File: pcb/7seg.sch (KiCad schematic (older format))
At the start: 28 parts, among them Q10 2SC1815, Q11 2SC1815, Q12 2SC1815, Q13 2SC1815, Q14 2SC1815, Q9 2SC1815, U7 7seg-2digit-ca, U8 7seg-2digit-ca, U9 7seg-2digit-ca

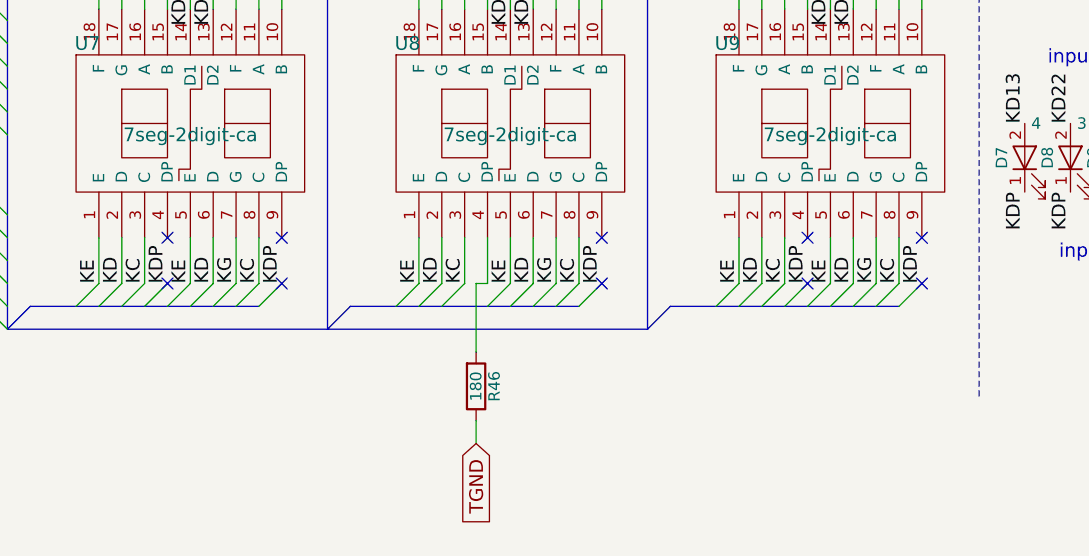
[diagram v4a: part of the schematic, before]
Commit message: wire に未接続の設定をしていたら文句を言われたので，wireの未接続を削除。
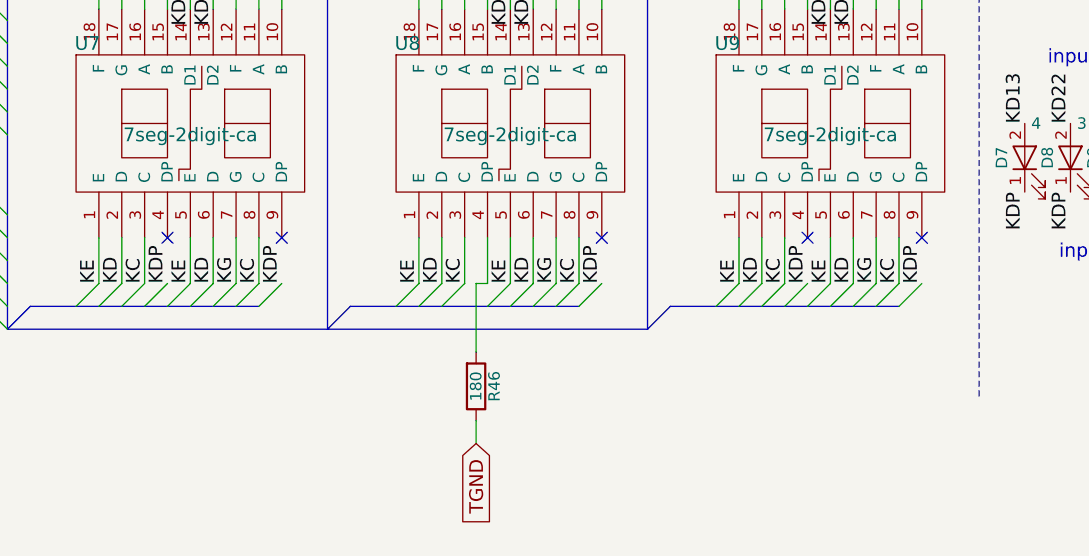
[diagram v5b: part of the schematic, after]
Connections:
- no-connect marks 10 -> 5
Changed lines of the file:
@@
 Entry Wire Line
 	5050 4000 4950 3900
-NoConn ~ 6250 3900
-NoConn ~ 5750 3900
-NoConn ~ 7650 3900
-NoConn ~ 9050 3900
 Text Label 4450 2450 2    60   ~ 0
 PB7
@@
 Text Notes 4450 3400 0    60   ~ 0
 input H.
-NoConn ~ 8550 3900
 Text Notes 9650 3800 0    60   ~ 0
 input L.
@@
 	1    0    0    -1
 $EndComp
-Wire Wire Line
-	3300 3900 4950 3900
-Wire Wire Line
-	3700 4000 4950 4000
-Wire Wire Line
-	2900 3800 4950 3800
-Wire Notes Line
-	9300 2100 9300 4400
-Wire Wire Line
-	7100 3900 7100 4200
-Wire Wire Line
-	7150 3900 7100 3900
-Wire Wire Line
-	7150 3700 7150 3900
-Wire Wire Line
-	4800 2450 4950 2450
-Wire Wire Line
-	1700 3500 4950 3500
-Wire Wire Line
-	2100 3600 4950 3600
-Wire Bus Line
-	7850 4100 7850 2550
-Wire Bus Line
-	7950 4000 8950 4000
-Wire Bus Line
-	7950 2450 8950 2450
-Wire Wire Line
-	8250 3900 8250 3700
-Wire Wire Line
-	8350 3900 8350 3700
-Wire Wire Line
-	8450 3900 8450 3700
-Wire Wire Line
-	8650 3900 8650 3700
-Wire Wire Line
-	8750 3900 8750 3700
-Wire Wire Line
-	8850 3900 8850 3700
-Wire Wire Line
-	8950 3900 8950 3700
-Wire Wire Line
-	8250 2550 8250 2700
-Wire Wire Line
-	8350 2550 8350 2700
-Wire Wire Line
-	8450 2550 8450 2700
-Wire Wire Line
-	8550 2550 8550 2700
-Wire Wire Line
-	8650 2550 8650 2700
-Wire Wire Line
-	8750 2550 8750 2700
-Wire Wire Line
-	8850 2550 8850 2700
-Wire Wire Line
-	8950 2550 8950 2700
-Wire Wire Line
-	9050 2550 9050 2700
-Wire Bus Line
-	5050 4100 7850 4100
-Wire Bus Line
-	6450 2550 6450 4100
-Wire Bus Line
-	6550 4000 7550 4000
-Wire Bus Line
-	6550 2450 7550 2450
-Wire Wire Line
-	6850 3900 6850 3700
-Wire Wire Line
-	6950 3900 6950 3700
-Wire Wire Line
-	7050 3900 7050 3700
-Wire Wire Line
-	7250 3900 7250 3700
-Wire Wire Line
-	7350 3900 7350 3700
-Wire Wire Line
-	7450 3900 7450 3700
-Wire Wire Line
-	7550 3900 7550 3700
-Wire Wire Line
-	6850 2550 6850 2700
-Wire Wire Line
-	6950 2550 6950 2700
-Wire Wire Line
-	7050 2550 7050 2700
-Wire Wire Line
-	7150 2550 7150 2700
-Wire Wire Line
-	7250 2550 7250 2700
-Wire Wire Line
-	7350 2550 7350 2700
-Wire Wire Line
-	7450 2550 7450 2700
-Wire Wire Line
-	7550 2550 7550 2700
-Wire Wire Line
-	7650 2550 7650 2700
-Wire Wire Line
-	4950 2650 4800 2650
-Wire Wire Line
-	4950 3150 4800 3150
-Wire Wire Line
-	4950 2550 4800 2550
-Wire Wire Line
-	4950 2950 4800 2950
-Wire Wire Line
-	4950 2850 4800 2850
-Wire Wire Line
-	4950 2750 4800 2750
-Wire Wire Line
-	4950 3050 4800 3050
-Wire Wire Line
-	4250 3150 4500 3150
-Wire Wire Line
-	4250 3050 4500 3050
-Wire Wire Line
-	4250 2950 4500 2950
-Wire Wire Line
-	4250 2850 4500 2850
-Wire Wire Line
-	4250 2750 4500 2750
-Wire Wire Line
-	4250 2650 4500 2650
-Wire Wire Line
-	4250 2550 4500 2550
-Wire Bus Line
-	5050 2550 5050 4100
-Wire Bus Line
-	5150 4000 6150 4000
-Wire Bus Line
-	5150 2450 6150 2450
-Wire Wire Line
-	5450 3900 5450 3700
-Wire Wire Line
-	5550 3900 5550 3700
-Wire Wire Line
-	5650 3900 5650 3700
-Wire Wire Line
-	5850 3900 5850 3700
-Wire Wire Line
-	5950 3900 5950 3700
-Wire Wire Line
-	6050 3900 6050 3700
-Wire Wire Line
-	6150 3900 6150 3700
-Wire Wire Line
-	5450 2550 5450 2700
-Wire Wire Line
-	5550 2550 5550 2700
-Wire Wire Line
-	5650 2550 5650 2700
-Wire Wire Line
-	5750 2550 5750 2700
-Wire Wire Line
-	5850 2550 5850 2700
-Wire Wire Line
-	5950 2550 5950 2700
-Wire Wire Line
-	6050 2550 6050 2700
-Wire Wire Line
-	6150 2550 6150 2700
-Wire Wire Line
-	6250 2550 6250 2700
-Wire Wire Line
-	4250 2450 4500 2450
-Wire Wire Line
-	7100 4600 7100 4500
-Wire Wire Line
-	1400 2650 1300 2650
-Wire Wire Line
-	1300 2750 1800 2750
-Wire Wire Line
-	1300 2850 2200 2850
-Wire Wire Line
-	1300 2950 2600 2950
-Wire Wire Line
-	3000 3050 1300 3050
-Wire Wire Line
-	1300 3150 3400 3150
-Wire Wire Line
-	850  3150 1000 3150
-Wire Wire Line
-	850  3050 1000 3050
-Wire Wire Line
-	1000 2650 850  2650
-Wire Wire Line
-	850  2750 1000 2750
-Wire Wire Line
-	1000 2850 850  2850
-Wire Wire Line
-	850  2950 1000 2950
-Wire Wire Line
-	1700 2850 1700 3500
-Wire Wire Line
-	2100 3600 2100 2950
-Wire Wire Line
-	2500 3700 2500 3050
-Wire Wire Line
-	2900 3800 2900 3150
-Wire Wire Line
-	3300 3250 3300 3900
-Wire Wire Line
-	3700 3350 3700 4000
-Wire Wire Line
-	3700 1800 3700 2950
-Wire Wire Line
-	1700 1950 3700 1950
-Wire Wire Line
-	3300 1950 3300 2850
-Wire Wire Line
-	2900 1950 2900 2750
-Connection ~ 3300 1950
-Wire Wire Line
-	2500 1950 2500 2650
-Connection ~ 2900 1950
-Wire Wire Line
-	2100 1950 2100 2550
-Connection ~ 2500 1950
-Wire Wire Line
-	1700 1950 1700 2450
-Connection ~ 2100 1950
-Connection ~ 3700 1950
 Text Label 4850 3700 2    60   ~ 0
 KD22
-Wire Wire Line
-	2500 3700 4950 3700
 Text Notes 800  3300 0    60   ~ 0
 flow ->
@@
 Text GLabel 3700 1800 2    60   Input ~ 0
 TVCC
+Wire Wire Line
+	3300 3900 4950 3900
+Wire Wire Line
+	3700 4000 4950 4000
+Wire Wire Line
+	2900 3800 4950 3800
+Wire Notes Line
+	9300 2100 9300 4400
+Wire Wire Line
+	7100 3900 7100 4200
+Wire Wire Line
+	7150 3900 7100 3900
+Wire Wire Line
+	7150 3700 7150 3900
+Wire Wire Line
+	4800 2450 4950 2450
+Wire Wire Line
+	1700 3500 4950 3500
+Wire Wire Line
+	2100 3600 4950 3600
+Wire Bus Line
+	7850 4100 7850 2550
+Wire Bus Line
+	7950 4000 8950 4000
+Wire Bus Line
+	7950 2450 8950 2450
+Wire Wire Line
+	8250 3900 8250 3700
+Wire Wire Line
+	8350 3900 8350 3700
+Wire Wire Line
+	8450 3900 8450 3700
+Wire Wire Line
+	8650 3900 8650 3700
+Wire Wire Line
+	8750 3900 8750 3700
+Wire Wire Line
+	8850 3900 8850 3700
+Wire Wire Line
+	8950 3900 8950 3700
+Wire Wire Line
+	8250 2550 8250 2700
+Wire Wire Line
+	8350 2550 8350 2700
+Wire Wire Line
+	8450 2550 8450 2700
+Wire Wire Line
+	8550 2550 8550 2700
+Wire Wire Line
+	8650 2550 8650 2700
+Wire Wire Line
+	8750 2550 8750 2700
+Wire Wire Line
+	8850 2550 8850 2700
+Wire Wire Line
+	8950 2550 8950 2700
+Wire Wire Line
+	9050 2550 9050 2700
+Wire Bus Line
+	5050 4100 7850 4100
+Wire Bus Line
+	6450 2550 6450 4100
+Wire Bus Line
+	6550 4000 7550 4000
+Wire Bus Line
+	6550 2450 7550 2450
+Wire Wire Line
+	6850 3900 6850 3700
+Wire Wire Line
+	6950 3900 6950 3700
+Wire Wire Line
+	7050 3900 7050 3700
+Wire Wire Line
+	7250 3900 7250 3700
+Wire Wire Line
+	7350 3900 7350 3700
+Wire Wire Line
+	7450 3900 7450 3700
+Wire Wire Line
+	7550 3900 7550 3700
+Wire Wire Line
+	6850 2550 6850 2700
+Wire Wire Line
+	6950 2550 6950 2700
+Wire Wire Line
+	7050 2550 7050 2700
+Wire Wire Line
+	7150 2550 7150 2700
+Wire Wire Line
+	7250 2550 7250 2700
+Wire Wire Line
+	7350 2550 7350 2700
+Wire Wire Line
+	7450 2550 7450 2700
+Wire Wire Line
+	7550 2550 7550 2700
+Wire Wire Line
+	7650 2550 7650 2700
+Wire Wire Line
+	4950 2650 4800 2650
+Wire Wire Line
+	4950 3150 4800 3150
+Wire Wire Line
+	4950 2550 4800 2550
+Wire Wire Line
+	4950 2950 4800 2950
+Wire Wire Line
+	4950 2850 4800 2850
+Wire Wire Line
+	4950 2750 4800 2750
+Wire Wire Line
+	4950 3050 4800 3050
+Wire Wire Line
+	4250 3150 4500 3150
+Wire Wire Line
+	4250 3050 4500 3050
+Wire Wire Line
+	4250 2950 4500 2950
+Wire Wire Line
+	4250 2850 4500 2850
+Wire Wire Line
+	4250 2750 4500 2750
+Wire Wire Line
+	4250 2650 4500 2650
+Wire Wire Line
+	4250 2550 4500 2550
+Wire Bus Line
+	5050 2550 5050 4100
+Wire Bus Line
+	5150 4000 6150 4000
+Wire Bus Line
+	5150 2450 6150 2450
+Wire Wire Line
+	5450 3900 5450 3700
+Wire Wire Line
+	5550 3900 5550 3700
+Wire Wire Line
+	5650 3900 5650 3700
+Wire Wire Line
+	5850 3900 5850 3700
+Wire Wire Line
+	5950 3900 5950 3700
+Wire Wire Line
+	6050 3900 6050 3700
+Wire Wire Line
+	6150 3900 6150 3700
+Wire Wire Line
+	5450 2550 5450 2700
+Wire Wire Line
+	5550 2550 5550 2700
+Wire Wire Line
+	5650 2550 5650 2700
+Wire Wire Line
+	5750 2550 5750 2700
+Wire Wire Line
+	5850 2550 5850 2700
+Wire Wire Line
+	5950 2550 5950 2700
+Wire Wire Line
+	6050 2550 6050 2700
+Wire Wire Line
+	6150 2550 6150 2700
+Wire Wire Line
+	6250 2550 6250 2700
+Wire Wire Line
+	4250 2450 4500 2450
+Wire Wire Line
+	7100 4600 7100 4500
+Wire Wire Line
+	1400 2650 1300 2650
+Wire Wire Line
+	1300 2750 1800 2750
+Wire Wire Line
+	1300 2850 2200 2850
+Wire Wire Line
+	1300 2950 2600 2950
+Wire Wire Line
+	3000 3050 1300 3050
+Wire Wire Line
+	1300 3150 3400 3150
+Wire Wire Line
+	850  3150 1000 3150
+Wire Wire Line
+	850  3050 1000 3050
+Wire Wire Line
+	1000 2650 850  2650
+Wire Wire Line
+	850  2750 1000 2750
+Wire Wire Line
+	1000 2850 850  2850
+Wire Wire Line
+	850  2950 1000 2950
+Wire Wire Line
+	1700 2850 1700 3500
+Wire Wire Line
+	2100 3600 2100 2950
+Wire Wire Line
+	2500 3700 2500 3050
+Wire Wire Line
+	2900 3800 2900 3150
+Wire Wire Line
+	3300 3250 3300 3900
+Wire Wire Line
+	3700 3350 3700 4000
+Wire Wire Line
+	3700 1800 3700 2950
+Wire Wire Line
+	1700 1950 3700 1950
+Wire Wire Line
+	3300 1950 3300 2850
+Wire Wire Line
+	2900 1950 2900 2750
+Connection ~ 3300 1950
+Wire Wire Line
+	2500 1950 2500 2650
+Connection ~ 2900 1950
+Wire Wire Line
+	2100 1950 2100 2550
+Connection ~ 2500 1950
+Wire Wire Line
+	1700 1950 1700 2450
+Connection ~ 2100 1950
+Connection ~ 3700 1950
+Wire Wire Line
+	2500 3700 4950 3700
 $EndSCHEMATC

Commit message: 抵抗を 6.3mm の 1 / 4 W の抵抗に変更。
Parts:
- D10, D7, D8, D9: footprint (none) -> LEDs:LED_D5.0mm
- R32, R33, R34, R35, R36, R37, R38, R39, R40, R41, R42, R43, R44, R45, R46: footprint (none) -> Resistors_THT:R_Axial_DIN0207_L6.3mm_D2.5mm_P7.62mm_Horizontal
- U7, U8, U9: footprint (none) -> freq-counter:PARA_LIGHT-552SRD
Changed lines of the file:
@@
 F 0 "U7" H 5400 3550 60  0000 C CNN
 F 1 "7seg-2digit-ca" H 5850 3150 60  0000 C CNN
-F 2 "" H 6100 3300 60  0001 C CNN
+F 2 "freq-counter:PARA_LIGHT-552SRD" H 6100 3300 60  0001 C CNN
 F 3 "" H 6100 3300 60  0001 C CNN
 	1    5850 3200
@@
 F 0 "R39" V 4700 2400 50  0000 C CNN
 F 1 "33" V 4650 2550 50  0000 C CNN
-F 2 "" V 4580 2550 50  0001 C CNN
+F 2 "Resistors_THT:R_Axial_DIN0207_L6.3mm_D2.5mm_P7.62mm_Horizontal" V 4580 2550 50  0001 C CNN
 F 3 "" H 4650 2550 50  0001 C CNN
 	1    4650 2550
@@
 F 0 "R40" V 4700 2500 50  0000 C CNN
 F 1 "33" V 4650 2650 50  0000 C CNN
-F 2 "" V 4580 2650 50  0001 C CNN
+F 2 "Resistors_THT:R_Axial_DIN0207_L6.3mm_D2.5mm_P7.62mm_Horizontal" V 4580 2650 50  0001 C CNN
 F 3 "" H 4650 2650 50  0001 C CNN
 	1    4650 2650
@@
 F 0 "R41" V 4700 2600 50  0000 C CNN
 F 1 "33" V 4650 2750 50  0000 C CNN
-F 2 "" V 4580 2750 50  0001 C CNN
+F 2 "Resistors_THT:R_Axial_DIN0207_L6.3mm_D2.5mm_P7.62mm_Horizontal" V 4580 2750 50  0001 C CNN
 F 3 "" H 4650 2750 50  0001 C CNN
 	1    4650 2750
@@
 F 0 "R42" V 4700 2700 50  0000 C CNN
 F 1 "33" V 4650 2850 50  0000 C CNN
-F 2 "" V 4580 2850 50  0001 C CNN
+F 2 "Resistors_THT:R_Axial_DIN0207_L6.3mm_D2.5mm_P7.62mm_Horizontal" V 4580 2850 50  0001 C CNN
 F 3 "" H 4650 2850 50  0001 C CNN
 	1    4650 2850
@@
 F 0 "R43" V 4700 2800 50  0000 C CNN
 F 1 "33" V 4650 2950 50  0000 C CNN
-F 2 "" V 4580 2950 50  0001 C CNN
+F 2 "Resistors_THT:R_Axial_DIN0207_L6.3mm_D2.5mm_P7.62mm_Horizontal" V 4580 2950 50  0001 C CNN
 F 3 "" H 4650 2950 50  0001 C CNN
 	1    4650 2950
@@
 F 0 "R44" V 4700 2900 50  0000 C CNN
 F 1 "33" V 4650 3050 50  0000 C CNN
-F 2 "" V 4580 3050 50  0001 C CNN
+F 2 "Resistors_THT:R_Axial_DIN0207_L6.3mm_D2.5mm_P7.62mm_Horizontal" V 4580 3050 50  0001 C CNN
 F 3 "" H 4650 3050 50  0001 C CNN
 	1    4650 3050
@@
 F 0 "R45" V 4700 3000 50  0000 C CNN
 F 1 "33" V 4650 3150 50  0000 C CNN
-F 2 "" V 4580 3150 50  0001 C CNN
+F 2 "Resistors_THT:R_Axial_DIN0207_L6.3mm_D2.5mm_P7.62mm_Horizontal" V 4580 3150 50  0001 C CNN
 F 3 "" H 4650 3150 50  0001 C CNN
 	1    4650 3150
@@
 F 0 "U8" H 6800 3550 60  0000 C CNN
 F 1 "7seg-2digit-ca" H 7250 3150 60  0000 C CNN
-F 2 "" H 7500 3300 60  0001 C CNN
+F 2 "freq-counter:PARA_LIGHT-552SRD" H 7500 3300 60  0001 C CNN
 F 3 "" H 7500 3300 60  0001 C CNN
 	1    7250 3200
@@
 F 0 "U9" H 8200 3550 60  0000 C CNN
 F 1 "7seg-2digit-ca" H 8650 3150 60  0000 C CNN
-F 2 "" H 8900 3300 60  0001 C CNN
+F 2 "freq-counter:PARA_LIGHT-552SRD" H 8900 3300 60  0001 C CNN
 F 3 "" H 8900 3300 60  0001 C CNN
 	1    8650 3200
@@
 F 0 "D8" H 9700 3450 50  0000 C CNN
 F 1 "3" V 9850 3300 50  0000 C CNN
-F 2 "" H 9700 3350 50  0001 C CNN
+F 2 "LEDs:LED_D5.0mm" H 9700 3350 50  0001 C CNN
 F 3 "" H 9700 3350 50  0001 C CNN
 	1    9700 3350
@@
 F 0 "D9" H 9900 3450 50  0000 C CNN
 F 1 "2" V 10050 3300 50  0000 C CNN
-F 2 "" H 9900 3350 50  0001 C CNN
+F 2 "LEDs:LED_D5.0mm" H 9900 3350 50  0001 C CNN
 F 3 "" H 9900 3350 50  0001 C CNN
 	1    9900 3350
@@
 F 0 "D7" H 9500 3450 50  0000 C CNN
 F 1 "4" V 9650 3300 50  0000 C CNN
-F 2 "" H 9500 3350 50  0001 C CNN
+F 2 "LEDs:LED_D5.0mm" H 9500 3350 50  0001 C CNN
 F 3 "" H 9500 3350 50  0001 C CNN
 	1    9500 3350
@@
 F 0 "D10" H 10100 3450 50  0000 C CNN
 F 1 "1" V 10250 3300 50  0000 C CNN
-F 2 "" H 10100 3350 50  0001 C CNN
+F 2 "LEDs:LED_D5.0mm" H 10100 3350 50  0001 C CNN
 F 3 "" H 10100 3350 50  0001 C CNN
 	1    10100 3350
@@
 F 0 "R46" V 7180 4350 50  0000 C CNN
 F 1 "180" V 7100 4350 50  0000 C CNN
-F 2 "" V 7030 4350 50  0001 C CNN
+F 2 "Resistors_THT:R_Axial_DIN0207_L6.3mm_D2.5mm_P7.62mm_Horizontal" V 7030 4350 50  0001 C CNN
 F 3 "" H 7100 4350 50  0001 C CNN
 	1    7100 4350
@@
 F 0 "R38" V 4700 2300 50  0000 C CNN
 F 1 "330" V 4650 2450 50  0000 C CNN
-F 2 "" V 4580 2450 50  0001 C CNN
+F 2 "Resistors_THT:R_Axial_DIN0207_L6.3mm_D2.5mm_P7.62mm_Horizontal" V 4580 2450 50  0001 C CNN
 F 3 "" H 4650 2450 50  0001 C CNN
 	1    4650 2450
@@
 F 0 "R32" V 1200 2500 50  0000 C CNN
 F 1 "10k" V 1150 2650 50  0000 C CNN
-F 2 "" V 1080 2650 50  0001 C CNN
+F 2 "Resistors_THT:R_Axial_DIN0207_L6.3mm_D2.5mm_P7.62mm_Horizontal" V 1080 2650 50  0001 C CNN
 F 3 "" H 1150 2650 50  0001 C CNN
 	1    1150 2650
@@
 F 0 "R33" V 1200 2600 50  0000 C CNN
 F 1 "10k" V 1150 2750 50  0000 C CNN
-F 2 "" V 1080 2750 50  0001 C CNN
+F 2 "Resistors_THT:R_Axial_DIN0207_L6.3mm_D2.5mm_P7.62mm_Horizontal" V 1080 2750 50  0001 C CNN
 F 3 "" H 1150 2750 50  0001 C CNN
 	1    1150 2750
@@
 F 0 "R34" V 1200 2700 50  0000 C CNN
 F 1 "10k" V 1150 2850 50  0000 C CNN
-F 2 "" V 1080 2850 50  0001 C CNN
+F 2 "Resistors_THT:R_Axial_DIN0207_L6.3mm_D2.5mm_P7.62mm_Horizontal" V 1080 2850 50  0001 C CNN
 F 3 "" H 1150 2850 50  0001 C CNN
 	1    1150 2850
@@
 F 0 "R35" V 1200 2800 50  0000 C CNN
 F 1 "10k" V 1150 2950 50  0000 C CNN
-F 2 "" V 1080 2950 50  0001 C CNN
+F 2 "Resistors_THT:R_Axial_DIN0207_L6.3mm_D2.5mm_P7.62mm_Horizontal" V 1080 2950 50  0001 C CNN
 F 3 "" H 1150 2950 50  0001 C CNN
 	1    1150 2950
@@
 F 0 "R36" V 1200 2900 50  0000 C CNN
 F 1 "10k" V 1150 3050 50  0000 C CNN
-F 2 "" V 1080 3050 50  0001 C CNN
+F 2 "Resistors_THT:R_Axial_DIN0207_L6.3mm_D2.5mm_P7.62mm_Horizontal" V 1080 3050 50  0001 C CNN
 F 3 "" H 1150 3050 50  0001 C CNN
 	1    1150 3050
@@
 F 0 "R37" V 1200 3000 50  0000 C CNN
 F 1 "10k" V 1150 3150 50  0000 C CNN
-F 2 "" V 1080 3150 50  0001 C CNN
+F 2 "Resistors_THT:R_Axial_DIN0207_L6.3mm_D2.5mm_P7.62mm_Horizontal" V 1080 3150 50  0001 C CNN
 F 3 "" H 1150 3150 50  0001 C CNN
 	1    1150 3150

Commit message: 2SC1815 の footprint を，足の間隔が0.1inchのfootprintに変更。
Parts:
- Q10, Q11, Q12, Q13, Q14, Q9: footprint TO_SOT_Packages_THT:TO-92_Molded_Narrow -> TO_SOT_Packages_THT:TO-92_Inline_Wide
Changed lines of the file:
@@
 F 0 "Q9" H 1450 2750 50  0000 L CNN
 F 1 "2SC1815" H 1350 2850 50  0000 L CNN
-F 2 "TO_SOT_Packages_THT:TO-92_Molded_Narrow" H 1800 2575 50  0001 L CIN
+F 2 "TO_SOT_Packages_THT:TO-92_Inline_Wide" H 1800 2575 50  0001 L CIN
 F 3 "" H 1600 2650 50  0001 L CNN
 	1    1600 2650
@@
 F 0 "Q10" H 1850 2850 50  0000 L CNN
 F 1 "2SC1815" H 1750 2950 50  0000 L CNN
-F 2 "TO_SOT_Packages_THT:TO-92_Molded_Narrow" H 2200 2675 50  0001 L CIN
+F 2 "TO_SOT_Packages_THT:TO-92_Inline_Wide" H 2200 2675 50  0001 L CIN
 F 3 "" H 2000 2750 50  0001 L CNN
 	1    2000 2750
@@
 F 0 "Q11" H 2250 2950 50  0000 L CNN
 F 1 "2SC1815" H 2150 3050 50  0000 L CNN
-F 2 "TO_SOT_Packages_THT:TO-92_Molded_Narrow" H 2600 2775 50  0001 L CIN
+F 2 "TO_SOT_Packages_THT:TO-92_Inline_Wide" H 2600 2775 50  0001 L CIN
 F 3 "" H 2400 2850 50  0001 L CNN
 	1    2400 2850
@@
 F 0 "Q12" H 2650 3050 50  0000 L CNN
 F 1 "2SC1815" H 2550 3150 50  0000 L CNN
-F 2 "TO_SOT_Packages_THT:TO-92_Molded_Narrow" H 3000 2875 50  0001 L CIN
+F 2 "TO_SOT_Packages_THT:TO-92_Inline_Wide" H 3000 2875 50  0001 L CIN
 F 3 "" H 2800 2950 50  0001 L CNN
 	1    2800 2950
@@
 F 0 "Q13" H 3050 3150 50  0000 L CNN
 F 1 "2SC1815" H 2950 3250 50  0000 L CNN
-F 2 "TO_SOT_Packages_THT:TO-92_Molded_Narrow" H 3400 2975 50  0001 L CIN
+F 2 "TO_SOT_Packages_THT:TO-92_Inline_Wide" H 3400 2975 50  0001 L CIN
 F 3 "" H 3200 3050 50  0001 L CNN
 	1    3200 3050
@@
 F 0 "Q14" H 3450 3250 50  0000 L CNN
 F 1 "2SC1815" H 3350 3350 50  0000 L CNN
-F 2 "TO_SOT_Packages_THT:TO-92_Molded_Narrow" H 3800 3075 50  0001 L CIN
+F 2 "TO_SOT_Packages_THT:TO-92_Inline_Wide" H 3800 3075 50  0001 L CIN
 F 3 "" H 3600 3150 50  0001 L CNN
 	1    3600 3150
